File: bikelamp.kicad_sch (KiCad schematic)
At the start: 9 parts, among them SW1 SW_MEC_5E, U1 WT51822-S4AT

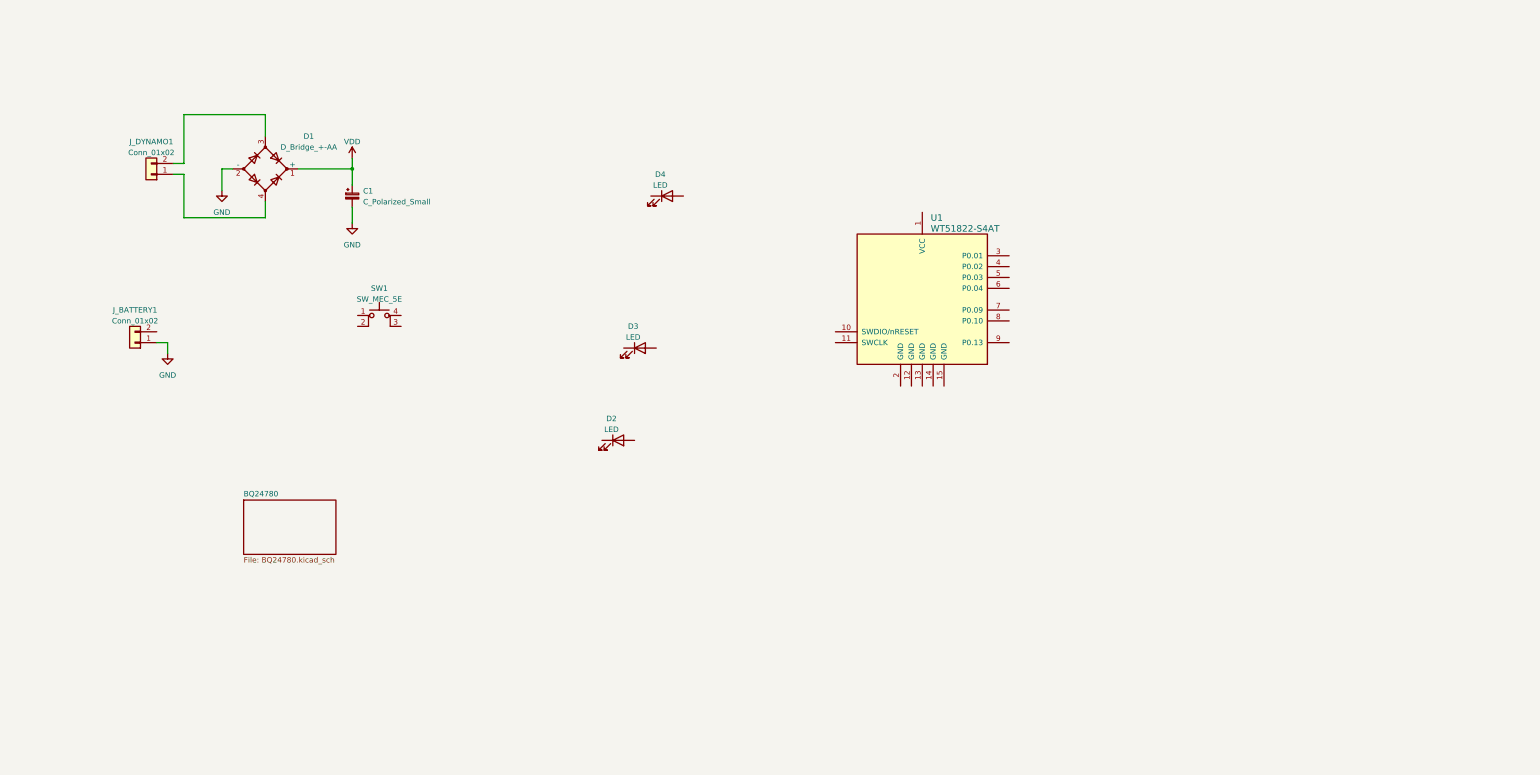
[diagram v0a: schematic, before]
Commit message: Replaced BLE module with YJ-xxx
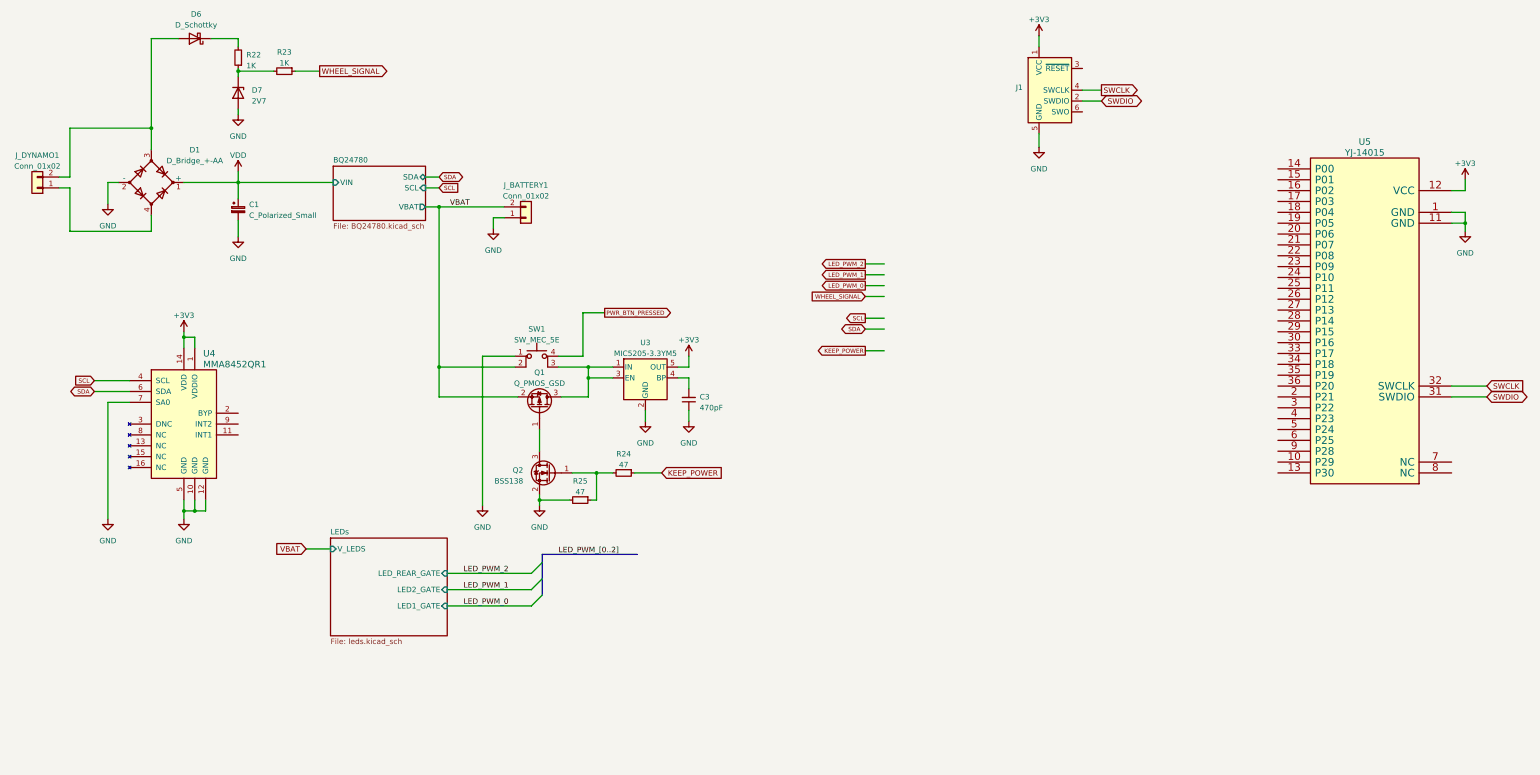
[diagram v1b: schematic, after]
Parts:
- removed D2, D3, D4: LED, LED_SMD:LED_1W_3W_R8, symbol Device:LED
- removed U1: WT51822-S4AT, libs:NRF51822-04, symbol wireless-modules:WT51822-S4AT
- added C3: 470pF, Resistor_SMD:R_0603_1608Metric, symbol Device:C_Small
- added D6: D_Schottky, symbol Device:D_Schottky
- added D7: 2V7, symbol Device:D_Zener
- added J1: Conn_ARM_SWD_TagConnect_TC2030-NL, Connector:Tag-Connect_TC2030-IDC-NL_2x03_P1.27mm_Vertical, symbol Connector:Conn_ARM_SWD_TagConnect_TC2030-NL
- added Q1: Q_PMOS_GSD, Package_TO_SOT_SMD:SOT-23, symbol Device:Q_PMOS_GSD
- added Q2: BSS138, Package_TO_SOT_SMD:SOT-23, symbol Transistor_FET:BSS138
- added R22, R23: 1K, symbol Device:R_Small
- added R24, R25: 47, symbol Device:R_Small
- added U3: MIC5205-3.3YM5, Package_TO_SOT_SMD:SOT-23-5, symbol Regulator_Linear:MIC5205-3.3YM5
- added U4: MMA8452QR1, digikey-footprints:VQFN-16_3x3mm, symbol dk_Motion-Sensors-Accelerometers:MMA8452QR1
- added U5: YJ-14015, footprints:YJ-14015, symbol YJ-14015:YJ-14015
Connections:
- net GND: now also SW1.1, C3.1, D7.2 (A), J1.5 (GND), Q2.2 (S), R25.2, U3.2 (GND), U4.10 (GND), U4.12 (GND), U4.5 (GND), U4.7 (SA0), U5.1 (GND), U5.11 (GND)
- net at D1.3, J_DYNAMO1.2 (Pin_2): now also D6.2 (A)
- net VBAT: now reaches J_BATTERY1.2 (Pin_2)
- net VBAT: now also SW1.2, Q1.2 (S)
- net at SW1.3 (K): now also Q1.3 (D), U3.1 (IN), U3.3 (EN)
- net PWR_BTN_PRESSED: now reaches SW1.4 (A)
- new net: Q2.1 (G), R24.2, R25.1
- new net: D7.1 (K), R22.1, R23.2
- new net: Q1.1 (G), Q2.3 (D)
- new net: D6.1 (K), R22.2
- new net: C3.2, U3.4 (BP)
- new net +3V3: J1.1 (VCC), U3.5 (OUT), U4.1 (VDDIO), U4.14 (VDD), U5.12 (VCC)
- new net KEEP_POWER: R24.1
- new net SCL: U4.4 (SCL)
- new net SDA: U4.6 (SDA)
- new net SWCLK: J1.4 (SWCLK), U5.32 (SWCLK)
- new net SWDIO: J1.2 (SWDIO), U5.31 (SWDIO)
- new net WHEEL_SIGNAL: R23.1
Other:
- added sheet LEDs (leds.kicad_sch)
- sheet BQ24780 ports: added SCL, SDA, VBAT, VIN; removed none
- moved on the sheet: C1, D1, J_BATTERY1, J_DYNAMO1, SW1

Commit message: Working on contours
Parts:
- added C3: 100nF, Capacitor_SMD:C_0603_1608Metric, symbol Device:C_Small
- added C3 (x2): 5pF, Capacitor_SMD:C_0603_1608Metric, symbol Device:C_Small
- added U1: MCP79402T-xSN, Package_SO:SO-8_3.9x4.9mm_P1.27mm, symbol Timer_RTC:MCP79402T-xSN
- added U6: MC-306, footprints:MC-306, symbol MC-306:MC-306
- C1: footprint (none) -> footprints:BQ24780SRUYR
- C3: footprint Resistor_SMD:R_0603_1608Metric -> Capacitor_SMD:C_0603_1608Metric
- R22, R23, R24, R25: footprint (none) -> Resistor_SMD:R_0603_1608Metric
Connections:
- net +3V3: now also U1.8 (VCC)
- net GND: now also C3.1, C3.1, C3.1, U1.4 (VSS)
- net KEEP_POWER: now also U5.22 (P08)
- net LED_PWM_0: now also U5.16 (P02)
- net LED_PWM_1: now also U5.15 (P01)
- net LED_PWM_2: now also U5.14 (P00)
- net PWR_BTN_PRESSED: now also U5.21 (P07)
- net SCL: now also U5.19 (P05), U1.6 (SCL)
- net SDA: now also U5.20 (P06), U1.5 (SDA)
- net WHEEL_SIGNAL: now also U5.17 (P03)
- net MMA8452_INT1: now reaches U4.11 (INT1)
- net MMA8452_INT1: now also U5.23 (P09)
- net at U4.2 (BYP): now also C3.2
- net MMA8452_INT2: now reaches U4.9 (INT2)
- net MMA8452_INT2: now also U5.24 (P10)
- new net: C3.2, U1.2 (X2), U6.1 (D1)
- new net: C3.2, U1.1 (X1), U6.4 (D4)
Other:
- moved on the sheet: J1, U5

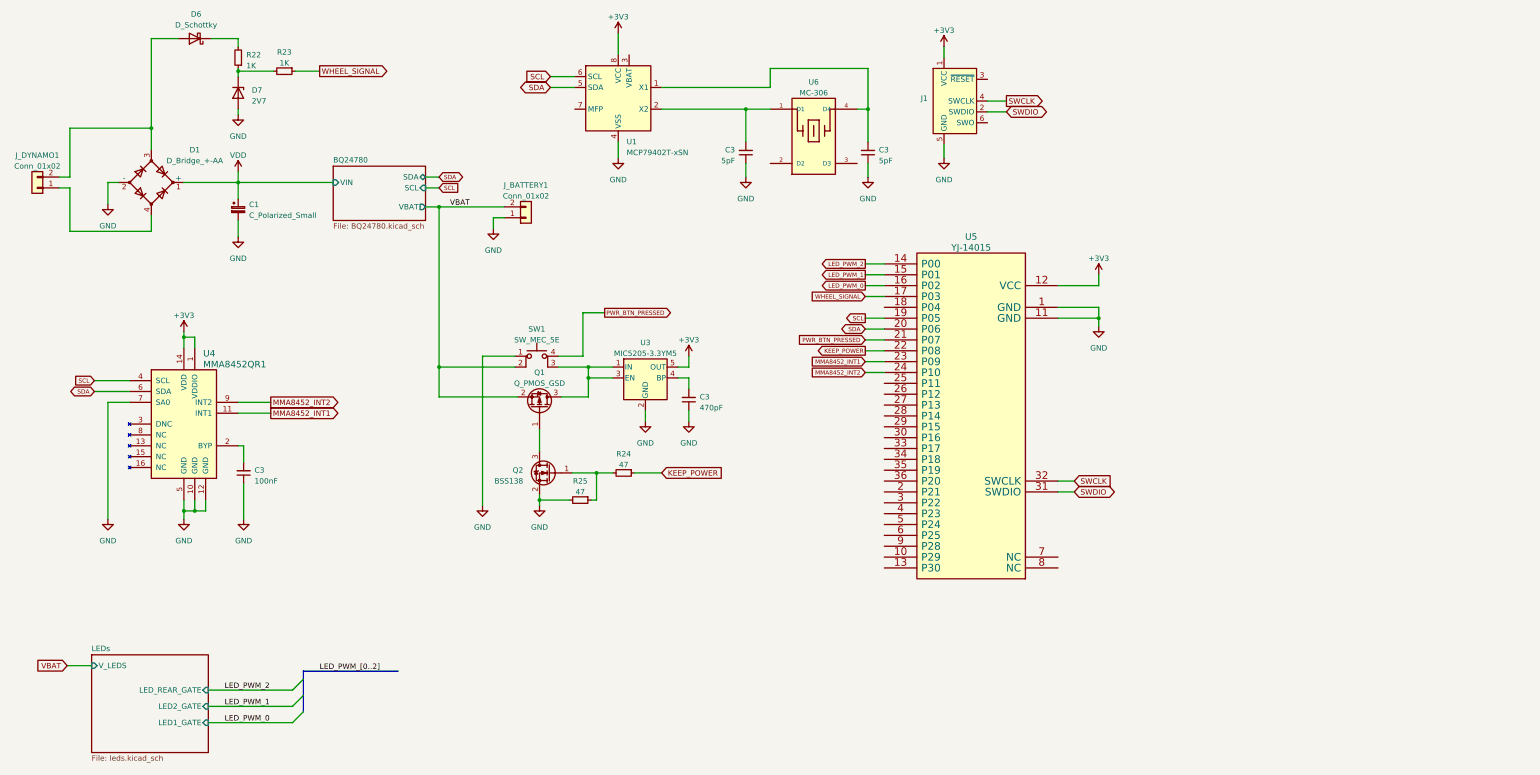
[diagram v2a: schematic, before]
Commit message: Added gate protection circuit to the SCH
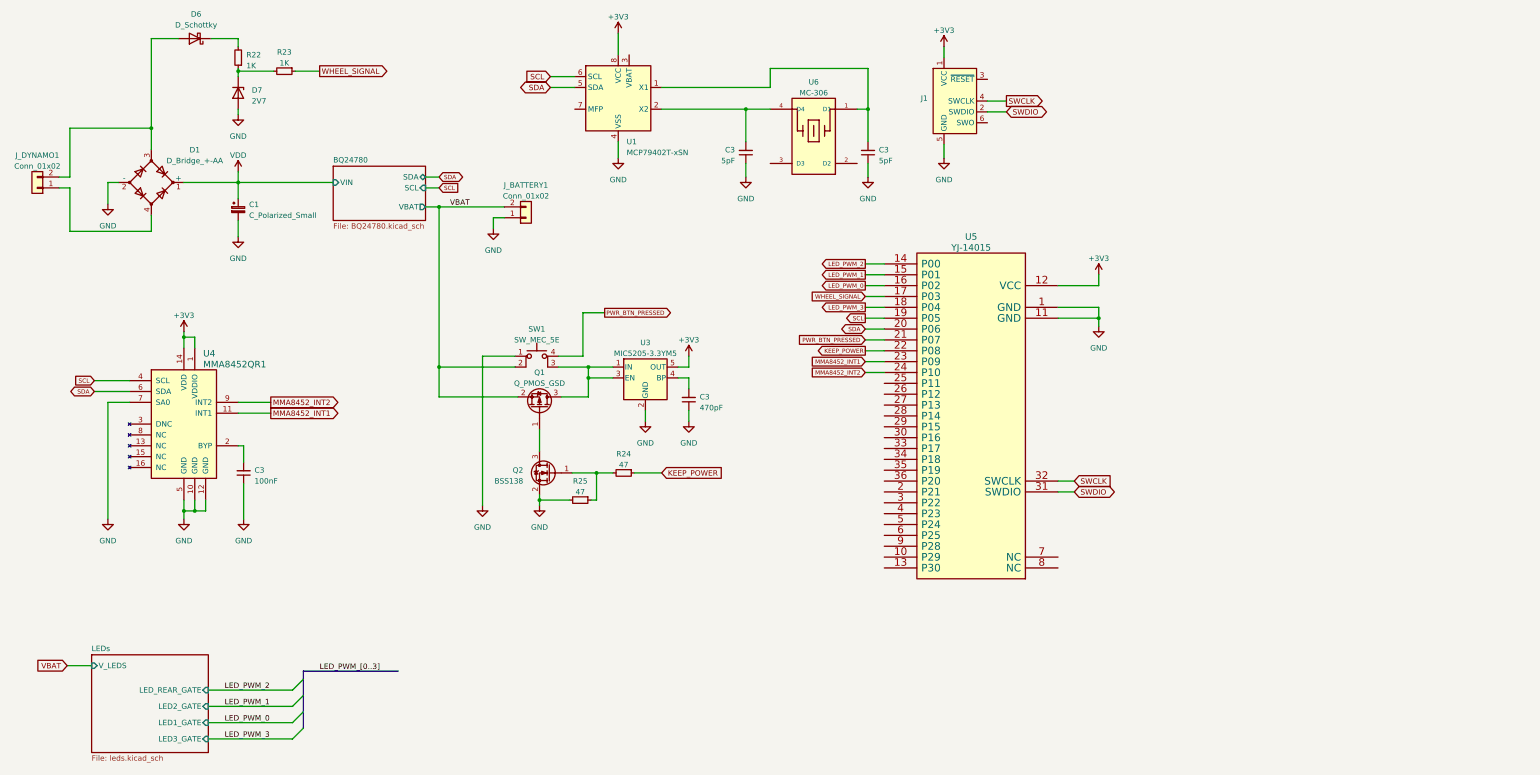
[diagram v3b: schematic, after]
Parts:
- C1: footprint footprints:BQ24780SRUYR -> (none)
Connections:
- net at C3.2, U1.2 (X2): now also U6.4 (D4); no longer U6.1 (D1)
- net at C3.2, U1.1 (X1): now also U6.1 (D1); no longer U6.4 (D4)
- net LED_PWM_3: now reaches U5.18 (P04)
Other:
- sheet LEDs ports: added LED3_GATE; removed none
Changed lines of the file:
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@@
   (junction (at 150.495 99.695) (diameter 0) (color 0 0 0 0)
   )
+  (bus_entry (at 81.28 186.69) (size 2.54 -2.54)
+    (stroke (width 0) (type default))
+  )
   (bus_entry (at 81.28 182.88) (size 2.54 -2.54)
     (stroke (width 0) (type default))
@@
     (stroke (width 0) (type default))
   )
+  (wire (pts (xy 61.595 186.69) (xy 81.28 186.69))
+    (stroke (width 0) (type default))
+  )
   (wire (pts (xy 130.81 64.77) (xy 128.27 64.77))
     (stroke (width 0) (type default))
@@
     (stroke (width 0) (type default))
   )
+  (wire (pts (xy 215.265 85.725) (xy 219.71 85.725))
+    (stroke (width 0) (type default))
+  )
   (wire (pts (xy 146.685 124.46) (xy 152.4 124.46))
     (stroke (width 0) (type default))
@@
   )
   (wire (pts (xy 141.605 31.75) (xy 147.32 31.75))
+    (stroke (width 0) (type default))
+  )
+  (bus (pts (xy 83.82 180.34) (xy 83.82 184.15))
     (stroke (width 0) (type default))
   )
@@
     (effects (font (size 1.27 1.27)) (justify left bottom))
   )
-  (label "LED_PWM_[0..2]" (at 87.63 170.815 0) (fields_autoplaced)
+  (label "LED_PWM_[0..3]" (at 87.63 170.815 0) (fields_autoplaced)
     (effects (font (size 1.27 1.27)) (justify left bottom))
   )
   (label "VBAT" (at 118.11 62.23 0) (fields_autoplaced)
+    (effects (font (size 1.27 1.27)) (justify left bottom))
+  )
+  (label "LED_PWM_3" (at 65.405 186.69 0) (fields_autoplaced)
     (effects (font (size 1.27 1.27)) (justify left bottom))
   )
@@
     )
   )
+  (global_label "LED_PWM_3" (shape output) (at 215.265 85.725 180) (fields_autoplaced)
+    (effects (font (size 1 1)) (justify right))
+    (property "Intersheetrefs" "${INTERSHEET_REFS}" (at 204.5008 85.725 0)
+      (effects (font (size 1.27 1.27)) (justify right) hide)
+    )
+  )
   (global_label "KEEP_POWER" (shape input) (at 167.64 124.46 0) (fields_autoplaced)
     (effects (font (size 1.27 1.27)) (justify left))
@@
     )
   )
-  (symbol (lib_id "MC-306:MC-306") (at 203.2 44.45 0) (unit 1)
-    (in_bom yes) (on_board yes) (dnp no) (fields_autoplaced)
+  (symbol (lib_id "MC-306:MC-306") (at 203.2 44.45 0) (mirror y) (unit 1)
+    (in_bom yes) (on_board yes) (dnp no)
     (property "Reference" "U6" (at 203.2 33.02 0)
       (effects (font (size 1.27 1.27)))
@@
       (effects (font (size 1.27 1.27)) (justify left))
     )
-    (property "Footprint" "footprints:BQ24780SRUYR" (at 68.58 62.865 0)
+    (property "Footprint" "" (at 68.58 62.865 0)
       (effects (font (size 1.27 1.27)) hide)
     )
@@
       (effects (font (size 1.27 1.27)) (justify right))
     )
+    (pin "LED3_GATE" input (at 61.595 186.69 0)
+      (effects (font (size 1.27 1.27)) (justify right))
+    )

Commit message: ERC pass
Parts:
- U6: footprint footprints:MC-306 -> MC-306
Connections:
- net TB_STAT: now reaches U5.25 (P11)
- net ACOK: now reaches U5.26 (P12)
- no-connect marks 0 -> 24
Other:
- sheet BQ24780 ports: added ACOK, TB_STAT; removed none
- moved on the sheet: C1, C3, D1, J1, J_BATTERY1, J_DYNAMO1, Q1, Q2, R22, R23, SW1, U3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

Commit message: Board routed
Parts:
- removed D7: 2V7, symbol Device:D_Zener
- removed J_DYNAMO1: Conn_01x02, symbol Connector_Generic:Conn_01x02
- added C5 (x3): 100nF, Capacitor_SMD:C_0603_1608Metric, symbol Device:C_Small
- added D8: BZV55C2V7, Diode_SMD:D_MiniMELF, symbol Diode:BZV55C2V7
- added J2: Conn_01x04_Pin, Connector_Phoenix_MC:PhoenixContact_MCV_1,5_4-GF-3.5_1x04_P3.50mm_Vertical_ThreadedFlange_MountHole, symbol Connector:Conn_01x04_Pin
- C1: value C_Polarized_Small -> 100uF; footprint (none) -> Capacitor_SMD:CP_Elec_6.3x5.7; Voltage (none) -> 35V
- D1: footprint (none) -> Diode_SMD:Diode_Bridge_Diotec_ABS
- D6: footprint (none) -> Diode_SMD:D_MicroMELF
- J_BATTERY1: footprint (none) -> Connector_JST:JST_VH_B2P-VH-FB-B_1x02_P3.96mm_Vertical
- U4: footprint digikey-footprints:VQFN-16_3x3mm -> footprints:VQFN-16_3x3mm
- U6: footprint MC-306 -> footprints:MC-306
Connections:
- net +3V3: now also C5.2, C5.2, C5.2
- net GND: now also C5.1, C5.1, C5.1, D8.2 (A)
- net LED_PWM_0: now also U5.15 (P01); no longer U5.16 (P02)
- net LED_PWM_1: now also U5.16 (P02); no longer U5.15 (P01)
- net WHEEL_SIGNAL: now also U5.27 (P13); no longer U5.17 (P03)
- net at R22.1, R23.2: now also D8.1 (K)
- net at D1.4: now also J2.1 (Pin_1)
- net at D1.3, D6.2 (A): now also J2.2 (Pin_2)
- new net REAR_LAMP_A: J2.3 (Pin_3)
- new net REAR_LAMP_K: J2.4 (Pin_4)
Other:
- sheet LEDs ports: added REAR_LEDS_A, REAR_LEDS_K; removed none
- moved on the sheet: D6, R22, R23
